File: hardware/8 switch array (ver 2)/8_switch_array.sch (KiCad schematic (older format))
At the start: 29 parts, among them J1 Conn_01x04, J10 Conn_01x02, J11 Conn_01x02, J2 Conn_01x04, J3 Conn_01x02, J4 Conn_01x02, J5 Conn_01x02, J6 Conn_01x02, J7 Conn_01x02, J8 Conn_01x02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

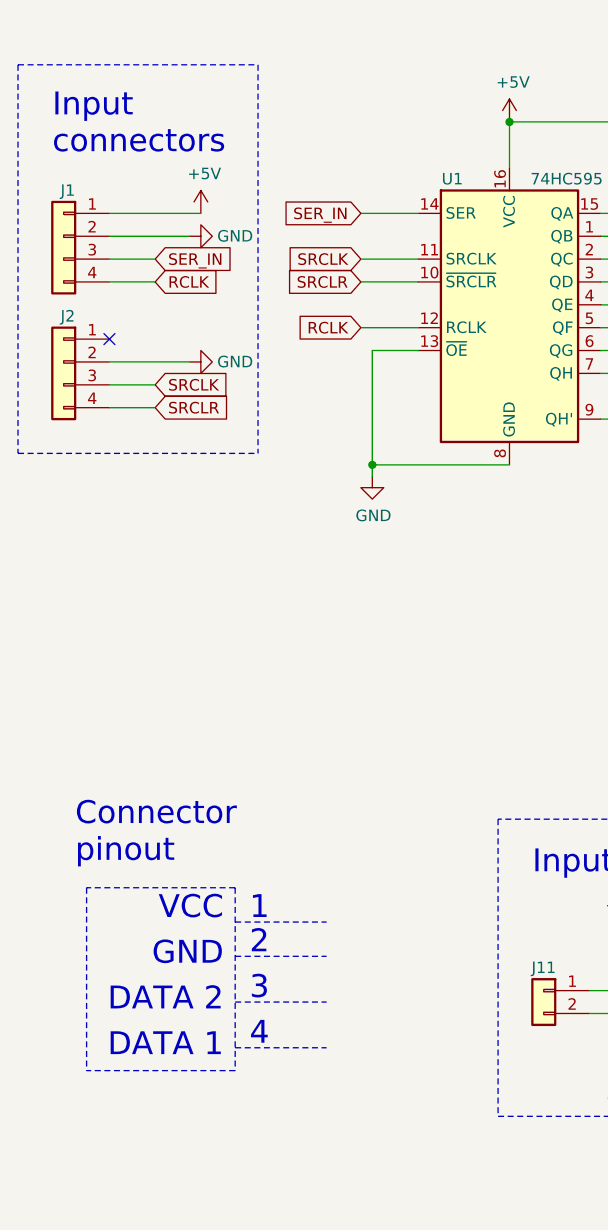
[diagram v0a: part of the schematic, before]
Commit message: update 8 switch array
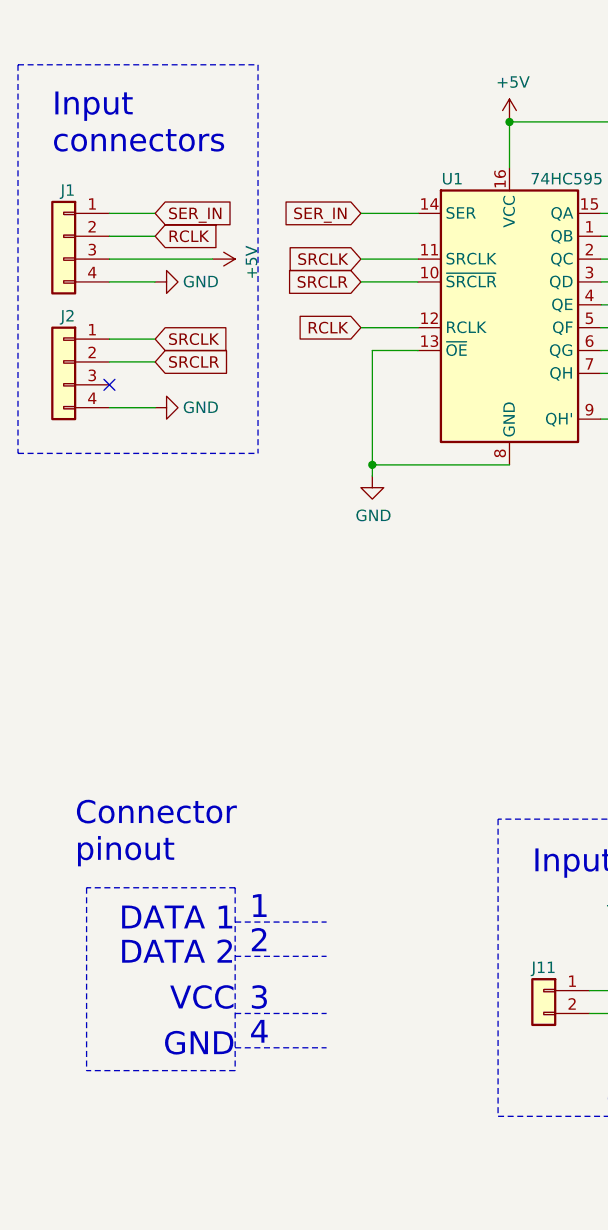
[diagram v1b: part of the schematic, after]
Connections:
- net +5V: now also J1.3 (Pin_3); no longer J1.1 (Pin_1)
- net GND: now also J1.4 (Pin_4), J2.4 (Pin_4); no longer J1.2 (Pin_2), J2.2 (Pin_2)
- net RCLK: now also J1.2 (Pin_2); no longer J1.4 (Pin_4)
- net SER_IN: now also J1.1 (Pin_1); no longer J1.3 (Pin_3)
- net SRCLK: now also J2.1 (Pin_1); no longer J2.3 (Pin_3)
- net SRCLR: now also J2.2 (Pin_2); no longer J2.4 (Pin_4)
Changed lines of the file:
@@
 EESchema Schematic File Version 4
-LIBS:8_switch_array-cache
 EELAYER 30 0
 EELAYER END
@@
 Wire Notes Line
 	5700 550  10600 550
-Text Notes 2150 5150 2    100  ~ 0
+Text Notes 2200 5550 2    100  ~ 0
 GND
-Text Notes 2150 4950 2    100  ~ 0
+Text Notes 2200 5350 2    100  ~ 0
 VCC
-Text Notes 2150 5350 2    100  ~ 0
+Text Notes 2200 5150 2    100  ~ 0
 DATA 2
-Text Notes 2150 5550 2    100  ~ 0
+Text Notes 2200 5000 2    100  ~ 0
 DATA 1
 Wire Notes Line style solid
@@
 	2200 4800 2200 5600
 Wire Notes Line style solid
+	2200 5100 2600 5100
+Wire Notes Line style solid
+	2200 4950 2600 4950
+Wire Notes Line style solid rgb(255, 0, 0)
+	2200 5350 2600 5350
+Wire Notes Line style solid rgb(0, 0, 0)
 	2200 5500 2600 5500
-Wire Notes Line style solid
-	2200 5300 2600 5300
-Wire Notes Line style solid rgb(255, 0, 0)
-	2200 4950 2600 4950
-Wire Notes Line style solid rgb(0, 0, 0)
-	2200 5100 2600 5100
 Text Notes 2350 4950 2    100  ~ 0
 1
 Text Notes 2350 5100 2    100  ~ 0
 2
-Text Notes 2350 5300 2    100  ~ 0
+Text Notes 2350 5350 2    100  ~ 0
 3
 Text Notes 2350 5500 2    100  ~ 0
@@
 Text GLabel 2750 1850 0    50   Input ~ 0
 SER_IN
-Text GLabel 1850 2050 2    50   Input ~ 0
+Text GLabel 1850 1850 2    50   Input ~ 0
 SER_IN
-Text GLabel 1850 2700 2    50   Input ~ 0
+Text GLabel 1850 2500 2    50   Input ~ 0
 SRCLR
 Wire Wire Line
 	2800 2450 2800 2950
-Text GLabel 1850 2150 2    50   Input ~ 0
+Text GLabel 1850 1950 2    50   Input ~ 0
 RCLK
 Text GLabel 2750 2350 0    50   Input ~ 0
@@
 L power:GND #PWR05
 U 1 1 5E319499
-P 2000 1950
-F 0 "#PWR05" H 2000 1700 50  0001 C CNN
-F 1 "GND" V 2000 1750 50  0000 C CNN
-F 2 "" H 2000 1950 50  0001 C CNN
-F 3 "" H 2000 1950 50  0001 C CNN
-	1    2000 1950
+P 1850 2150
+F 0 "#PWR05" H 1850 1900 50  0001 C CNN
+F 1 "GND" V 1850 1950 50  0000 C CNN
+F 2 "" H 1850 2150 50  0001 C CNN
+F 3 "" H 1850 2150 50  0001 C CNN
+	1    1850 2150
 	0    -1   -1   0
 $EndComp
@@
 L power:GND #PWR06
 U 1 1 5E32267D
-P 2000 2500
-F 0 "#PWR06" H 2000 2250 50  0001 C CNN
-F 1 "GND" V 2000 2300 50  0000 C CNN
-F 2 "" H 2000 2500 50  0001 C CNN
-F 3 "" H 2000 2500 50  0001 C CNN
-	1    2000 2500
+P 1850 2700
+F 0 "#PWR06" H 1850 2450 50  0001 C CNN
+F 1 "GND" V 1850 2500 50  0000 C CNN
+F 2 "" H 1850 2700 50  0001 C CNN
+F 3 "" H 1850 2700 50  0001 C CNN
+	1    1850 2700
 	0    -1   -1   0
 $EndComp
-Text GLabel 1850 2600 2    50   Input ~ 0
+Text GLabel 1850 2400 2    50   Input ~ 0
 SRCLK
-Wire Wire Line
-	1650 1950 2000 1950
-NoConn ~ 1650 2400
-Wire Wire Line
-	1650 2500 2000 2500
-Wire Wire Line
-	1650 2050 1850 2050
+NoConn ~ 1650 2600
 Wire Wire Line
 	1650 2150 1850 2150
-Wire Wire Line
-	1650 2600 1850 2600
 Wire Wire Line
 	1650 2700 1850 2700
@@
 L power:+5V #PWR0111
 U 1 1 5F43E1D7
-P 2050 1850
-F 0 "#PWR0111" H 2050 1700 50  0001 C CNN
-F 1 "+5V" H 2065 2023 50  0000 C CNN
-F 2 "" H 2050 1850 50  0001 C CNN
-F 3 "" H 2050 1850 50  0001 C CNN
-	1    2050 1850
-	1    0    0    -1
-$EndComp
-Wire Wire Line
-	1650 1850 2050 1850
+P 2100 2050
+F 0 "#PWR0111" H 2100 1900 50  0001 C CNN
+F 1 "+5V" H 2115 2223 50  0000 C CNN
+F 2 "" H 2100 2050 50  0001 C CNN
+F 3 "" H 2100 2050 50  0001 C CNN
+	1    2100 2050
+	0    1    1    0
+$EndComp
 $Comp
 L 74xx:74HC595 U1
@@
 Wire Wire Line
 	3800 2550 4000 2550
+Wire Wire Line
+	1650 2050 2100 2050
+Wire Wire Line
+	1650 1850 1850 1850
+Wire Wire Line
+	1650 1950 1850 1950
+Wire Wire Line
+	1650 2400 1850 2400
+Wire Wire Line
+	1650 2500 1850 2500
 $EndSCHEMATC

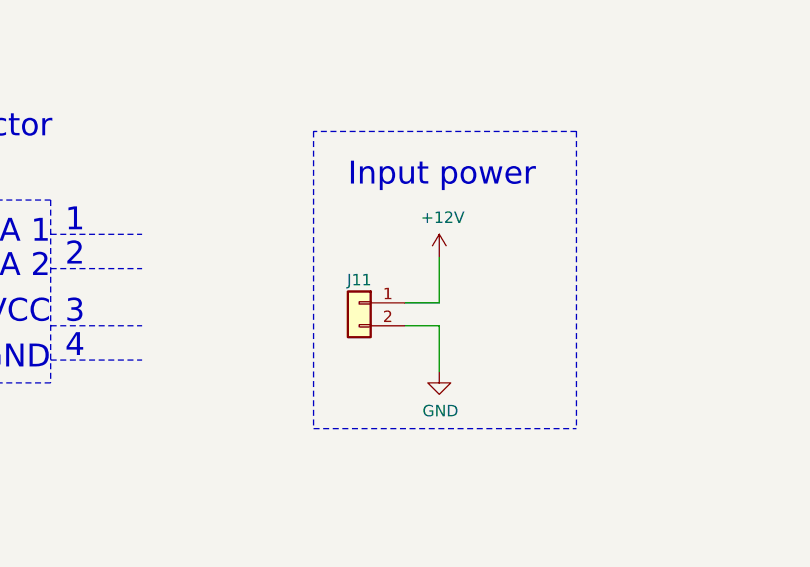
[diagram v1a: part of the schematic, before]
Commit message: Update on 12V5A system power line
- 12V5A power line is now represented by two connectors with 2 pins across all the modules
- all .png previews are updated. The central hub now has previews for schematics, PCB tracing and 3D model
- peltier module now has two 12V5A connectors with redesigned one side of the bridge. Now all MOSFETs can be equipped with heatsinks
- hum/temp sensor now has its connector position reversed to mimic Grove's one
- hum/temp and gas sensors now have a small BeeHive logo on front layer rather than one big on back layer
- hum/temp sensor now use only one layer for signals and one layer for ground
- switch arrays now have two connectors for 12V5A and 5V3A power lines
- switch arrays had their power lines better traced (no sharp turns)
- power supply (12V5A to 5V3A) now has two connectors for 12V5A power line
- one trace of power supply, which lies in between LM2596's legs, was narrowed to ensure that it will not be accidentally soldered or damaged during placement
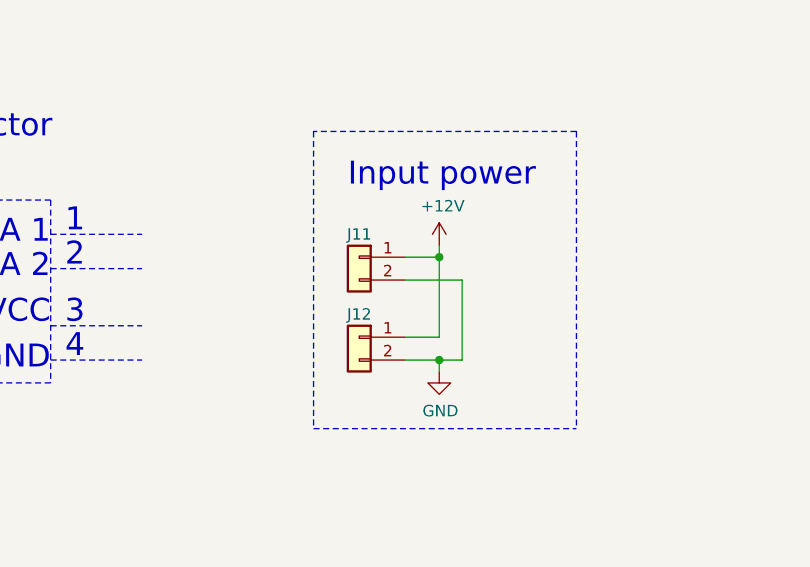
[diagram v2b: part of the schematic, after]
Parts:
- added J12: Conn_01x02, Connector_JST:JST_XH_B2B-XH-A_1x02_P2.50mm_Vertical, symbol Connector_Generic:Conn_01x02
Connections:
- net +12V: now also J12.1 (Pin_1)
- net GND: now also J12.2 (Pin_2)
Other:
- moved on the sheet: J11
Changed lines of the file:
@@
 L Connector_Generic:Conn_01x02 J11
 U 1 1 5E272691
-P 3550 5250
-F 0 "J11" H 3550 5350 50  0000 C CNN
-F 1 "Conn_01x02" H 3468 5016 50  0001 C CNN
-F 2 "Connector_JST:JST_XH_B2B-XH-A_1x02_P2.50mm_Vertical" H 3550 5250 50  0001 C CNN
-F 3 "~" H 3550 5250 50  0001 C CNN
-	1    3550 5250
+P 3550 5050
+F 0 "J11" H 3550 5150 50  0000 C CNN
+F 1 "Conn_01x02" H 3468 4816 50  0001 C CNN
+F 2 "Connector_JST:JST_XH_B2B-XH-A_1x02_P2.50mm_Vertical" H 3550 5050 50  0001 C CNN
+F 3 "~" H 3550 5050 50  0001 C CNN
+	1    3550 5050
 	-1   0    0    -1
 $EndComp
@@
 	1    0    0    -1
 $EndComp
-Wire Wire Line
-	3900 5350 3900 5550
-Wire Wire Line
-	3900 5250 3900 5050
 $Comp
 L Connector_Generic:Conn_01x02 J7
@@
 Wire Notes Line style solid
 	2200 4950 2600 4950
-Wire Notes Line style solid rgb(255, 0, 0)
-	2200 5350 2600 5350
 Wire Notes Line style solid rgb(0, 0, 0)
 	2200 5500 2600 5500
@@
 Text Notes 2350 5100 2    100  ~ 0
 2
-Text Notes 2350 5350 2    100  ~ 0
-3
 Text Notes 2350 5500 2    100  ~ 0
 4
@@
 	-1   0    0    -1
 $EndComp
-Wire Wire Line
-	3750 5350 3900 5350
-Wire Wire Line
-	3750 5250 3900 5250
 Text GLabel 2750 1850 0    50   Input ~ 0
 SER_IN
@@
 	10600 550  10600 6450
 $Comp
-L power:+12V #PWR0110
-U 1 1 5F43B8EF
-P 3900 5050
-F 0 "#PWR0110" H 3900 4900 50  0001 C CNN
-F 1 "+12V" H 3915 5223 50  0000 C CNN
-F 2 "" H 3900 5050 50  0001 C CNN
-F 3 "" H 3900 5050 50  0001 C CNN
-	1    3900 5050
-	1    0    0    -1
-$EndComp
-$Comp
 L power:+5V #PWR0111
 U 1 1 5F43E1D7
@@
 Wire Wire Line
 	1650 2500 1850 2500
+$Comp
+L power:+12V #PWR0110
+U 1 1 5F43B8EF
+P 3900 5000
+F 0 "#PWR0110" H 3900 4850 50  0001 C CNN
+F 1 "+12V" H 3915 5173 50  0000 C CNN
+F 2 "" H 3900 5000 50  0001 C CNN
+F 3 "" H 3900 5000 50  0001 C CNN
+	1    3900 5000
+	1    0    0    -1
+$EndComp
+Wire Wire Line
+	3750 5050 3900 5050
+Connection ~ 3900 5050
+Wire Wire Line
+	3900 5050 3900 5000
+Wire Wire Line
+	3750 5500 3900 5500
+Connection ~ 3900 5500
+Wire Wire Line
+	3900 5500 3900 5550
+Wire Wire Line
+	3750 5150 4000 5150
+Wire Wire Line
+	4000 5150 4000 5500
+Wire Wire Line
+	4000 5500 3900 5500
+Wire Wire Line
+	3900 5400 3750 5400
+Text Notes 2350 5350 2    100  ~ 0
+3
+Wire Notes Line style solid rgb(255, 0, 0)
+	2200 5350 2600 5350
+Wire Wire Line
+	3900 5050 3900 5400
+$Comp
+L Connector_Generic:Conn_01x02 J12
+U 1 1 5FD32169
+P 3550 5400
+F 0 "J12" H 3550 5500 50  0000 C CNN
+F 1 "Conn_01x02" H 3468 5166 50  0001 C CNN
+F 2 "Connector_JST:JST_XH_B2B-XH-A_1x02_P2.50mm_Vertical" H 3550 5400 50  0001 C CNN
+F 3 "~" H 3550 5400 50  0001 C CNN
+	1    3550 5400
+	-1   0    0    -1
+$EndComp
 $EndSCHEMATC
